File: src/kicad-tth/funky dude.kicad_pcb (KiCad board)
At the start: 2 copper layers, 57.2 x 37.5 mm, 33 parts, among them P1 CONN_2, P2 CONN_2, P3 CONN_2, SW1 SWITCH_INV, SW2 SWITCH_INV, U1 OP284

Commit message: version_2.0 initial
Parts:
- C3: value 11n -> 10n
- C6: value 50n -> 47n
- C9: value 47uf -> 47uF
- R2: value 500 -> 470

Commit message: 2014-10-22
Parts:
- removed C11: 47nf, User:C2-LARGE_PADS
- removed SW1, SW2: SWITCH_INV, User:SIL-3-LARGE_PADS
- C1, C13, C2, C3, C4, C5, C6: footprint User:C2-LARGE_PADS -> Custom:C2-LARGE_PADS
- C10, C12, C8, C9: footprint User:C1V7-LARGE_PADS -> Custom:C1V5-LARGE_PADS
- C7: value 47uf -> 1uF; footprint User:C1V7-LARGE_PADS -> Custom:C1V5-LARGE_PADS
- P1, P2, P3: footprint User:SIL-2-LARGE_PADS -> Custom:SIL-2-LARGE_PADS
- R1, R10, R11, R2, R3, R5, R6, R7, R9: footprint User:R3-LARGE_PADS -> Custom:R3-LARGE_PADS
- R4: footprint User:R4-LARGE_PADS -> Custom:R3-LARGE_PADS
- R8: value 1Meg -> 500; footprint User:R3-LARGE_PADS -> Custom:R3-LARGE_PADS
- RBASS1, RTREBLE1: footprint User:SIL-3-LARGE_PADS -> Custom:SIL-3-LARGE_PADS
- U1: footprint User:DIP-8_LARGE_PADS -> Custom:DIP-8_LARGE_PADS
- moved C12 41.7 mm to (176.5, 111.8), turned to 0 degrees
- moved RBASS1 29.5 mm to (164.5, 132.7), turned to 180 degrees
- moved C3 28.6 mm to (144.8, 130.2)
- moved R3 27.6 mm to (149.2, 120.7), turned to 270 degrees
- moved C7 25.6 mm to (148.6, 128.9)
- moved R11 21.6 mm to (167.0, 116.8), turned to 0 degrees
- moved R4 21.0 mm to (146.7, 120.7), turned to 270 degrees
- moved R6 14.8 mm to (167.0, 119.4), turned to 0 degrees
- moved C6 13.7 mm to (167.6, 122.6), turned to 0 degrees
- moved R9 11.9 mm to (175.9, 120.0), turned to 270 degrees
- moved C9 10.2 mm to (185.4, 115.6)
- moved P3 9.69 mm to (186.7, 128.3)
- moved P2 8.64 mm to (184.8, 121.3)
- moved C4 8.26 mm to (167.6, 126.4), turned to 0 degrees
- moved R10 8.13 mm to (167.0, 128.9), turned to 180 degrees
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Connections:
- C7 pad 2: Net-(C1-Pad1) -> GND
- R3 pad 2: Vref -> Net-(C7-Pad1)
- R8 pad 1: Net-(C7-Pad1) -> Net-(C4-Pad2)
- R8 pad 2: Vref -> Net-(C9-Pad1)
- RBASS1 pad 1: Net-(C9-Pad1) -> Net-(C4-Pad2)
- RBASS1 pad 2: Net-(C9-Pad1) -> Net-(C4-Pad2)
- RBASS1 pad 3: Net-(RBASS1-Pad3) -> Net-(C6-Pad1)
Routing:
- net GND: track 86.1 -> 0.00 mm
- net Net-(C1-Pad1): track 54.4 -> 4.45 mm
- net Net-(C11-Pad1): track 39.5 -> 0.00 mm
- net Net-(C6-Pad1): track 40.1 -> 19.3 mm
- net Net-(C3-Pad2): track 34.0 -> 14.9 mm
- net Net-(C7-Pad1): track 20.9 -> 3.44 mm
- net Net-(RBASS1-Pad3): track 15.8 -> 0.00 mm
- net Vref: track 49.5 -> 35.1 mm
- net Net-(C2-Pad1): track 38.8 -> 28.9 mm
- net Net-(C1-Pad2): track 11.7 -> 21.3 mm
- net Net-(C3-Pad1): track 13.2 -> 3.96 mm
- net Net-(C9-Pad1): track 19.2 -> 10.5 mm
- net +9V: track 55.3 -> 48.9 mm
- net Net-(C4-Pad2): track 72.1 -> 67.4 mm
- net Net-(C2-Pad2): track 28.6 -> 31.2 mm
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- added copper zone on F.Cu, net GND
- removed copper zone on B.Cu, net GND
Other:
- board size 57.2 x 37.5 mm -> 52.1 x 29.8 mm
- net class Default: clearance 0.508 -> 0.381; trace_width 0.762 -> 0.508; via_dia 1.016 -> 0.762; via_drill 0.635 -> 0.508
- rule trace_clearance: 0.508 -> 0.381
- board text added: "V2.0-t"
- board text added: "funky dude preamp v2.0-t www.dolganoff.com"
- board text removed: "V1-t"
- board text removed: "funky dude preamp v1-t www.dolganoff.com"

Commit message: 2014-10-23
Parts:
- moved P3 18.5 mm to (181.2, 110.6), turned to 180 degrees
- moved C13 6.87 mm to (178.4, 125.7), turned to 180 degrees
- moved C9 4.19 mm to (181.2, 115.7)
- moved C3 3.69 mm to (148.5, 130.3), turned to 0 degrees
- moved R8 3.52 mm to (177.2, 119.1), turned to 90 degrees
- moved R1 3.31 mm to (157.4, 120.4)
- moved R7 3.00 mm to (157.4, 123.3)
- moved C5 2.84 mm to (156.8, 126.4)
- moved C7 2.79 mm to (149.7, 126.4)
- moved C4 2.79 mm to (168.8, 123.8)
- moved U1 2.79 mm to (157.4, 113.0)
- moved C1 2.74 mm to (142.6, 118.1)
- moved R10 2.74 mm to (168.0, 126.4)
- moved RBASS1 2.73 mm to (165.7, 130.3)
- moved RTREBLE1 2.73 mm to (156.8, 130.3)
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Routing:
- net Net-(C4-Pad2): track 67.4 -> 57.1 mm
- net Vref: track 35.1 -> 26.8 mm
- net Net-(C9-Pad1): track 10.5 -> 2.83 mm
- net Net-(C3-Pad2): track 14.9 -> 9.82 mm
- net Net-(C3-Pad1): track 3.96 -> 8.79 mm
- net Net-(C12-Pad1): track 7.07 -> 5.09 mm
- net +9V: track 48.9 -> 47.5 mm
- net Net-(C1-Pad2): track 21.3 -> 20.1 mm
- net Net-(C9-Pad2): track 5.23 -> 4.68 mm
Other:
- board size 52.1 x 29.8 mm -> 45.2 x 27.9 mm
- board text added: "+"
- board text added: "Licenced under CERN OHL v1.2"
- board text added: "Open Hardware"
- board text added: "bass"
- board text added: "in"
- board text added: "out"
- board text added: "treble"
- board text removed: "V2.0-t"

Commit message: 2014-10-23.2 - PCB is routed
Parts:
- moved C10 0.63 mm to (178.7, 130.4)
- moved C9 0.51 mm to (181.2, 116.2)
- moved P3 0.51 mm to (181.2, 111.1)
- moved C1 0.46 mm to (142.4, 118.5)
- moved R3 0.36 mm to (150.0, 118.5)
- moved C4 0.36 mm to (168.5, 124.1)
- moved R4 0.36 mm to (147.4, 119.0)
- moved C6 0.28 mm to (168.5, 120.3)
- moved RGAIN1 0.28 mm to (147.4, 109.3)
- moved C13 0.28 mm to (178.2, 125.9)
- moved P2 0.25 mm to (182.2, 121.8)
- moved R10 0.25 mm to (168.0, 126.6)
- moved C2 0.25 mm to (167.3, 109.3)
- moved R11 0.25 mm to (168.5, 114.4)
- moved R2 0.25 mm to (144.9, 118.7)
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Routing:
- net Net-(C1-Pad2): track 20.1 -> 21.5 mm
- net Net-(C2-Pad2): track 31.0 -> 32.1 mm
- net +9V: track 47.5 -> 48.5 mm
- net Net-(C4-Pad1): track 41.9 -> 42.7 mm
- net Net-(C4-Pad2): track 57.1 -> 57.9 mm
- net Net-(C2-Pad1): track 28.5 -> 29.2 mm
- net Net-(C6-Pad1): track 19.4 -> 18.7 mm
- net Net-(C3-Pad1): track 8.79 -> 8.25 mm

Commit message: 2014-11-02 pcb changes
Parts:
- moved RBASS1 0.51 mm to (165.7, 129.9)
- moved RTREBLE1 0.51 mm to (156.8, 129.9)
- moved C13 0.25 mm to (178.2, 126.1)
- moved C4 0.25 mm to (168.5, 123.8)
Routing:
- net +9V: track 48.5 -> 23.4 mm
- net Net-(C4-Pad1): track 42.7 -> 40.9 mm
- net Net-(C5-Pad1): track 3.94 -> 3.43 mm
- added copper zone on B.Cu, net +9V
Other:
- outline, holes or cut-outs redrawn

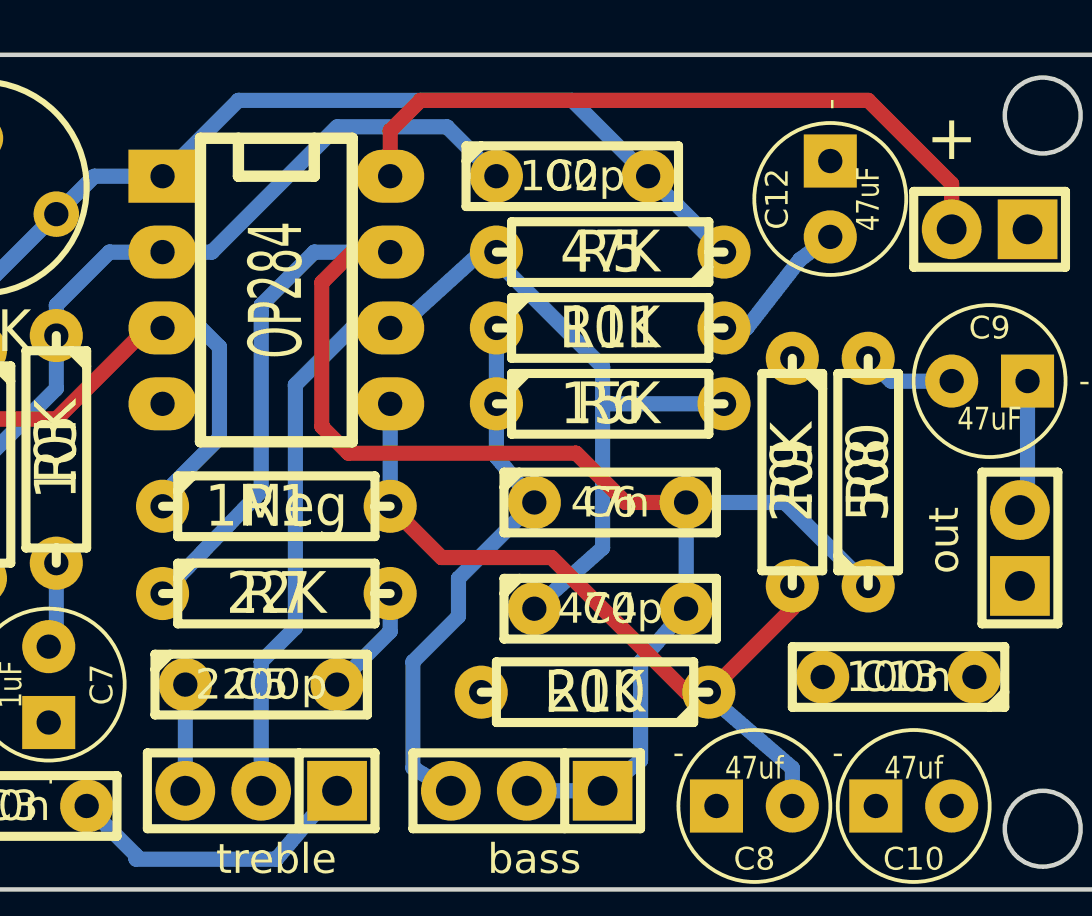
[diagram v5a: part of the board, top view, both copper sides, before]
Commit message: change to TLC2262
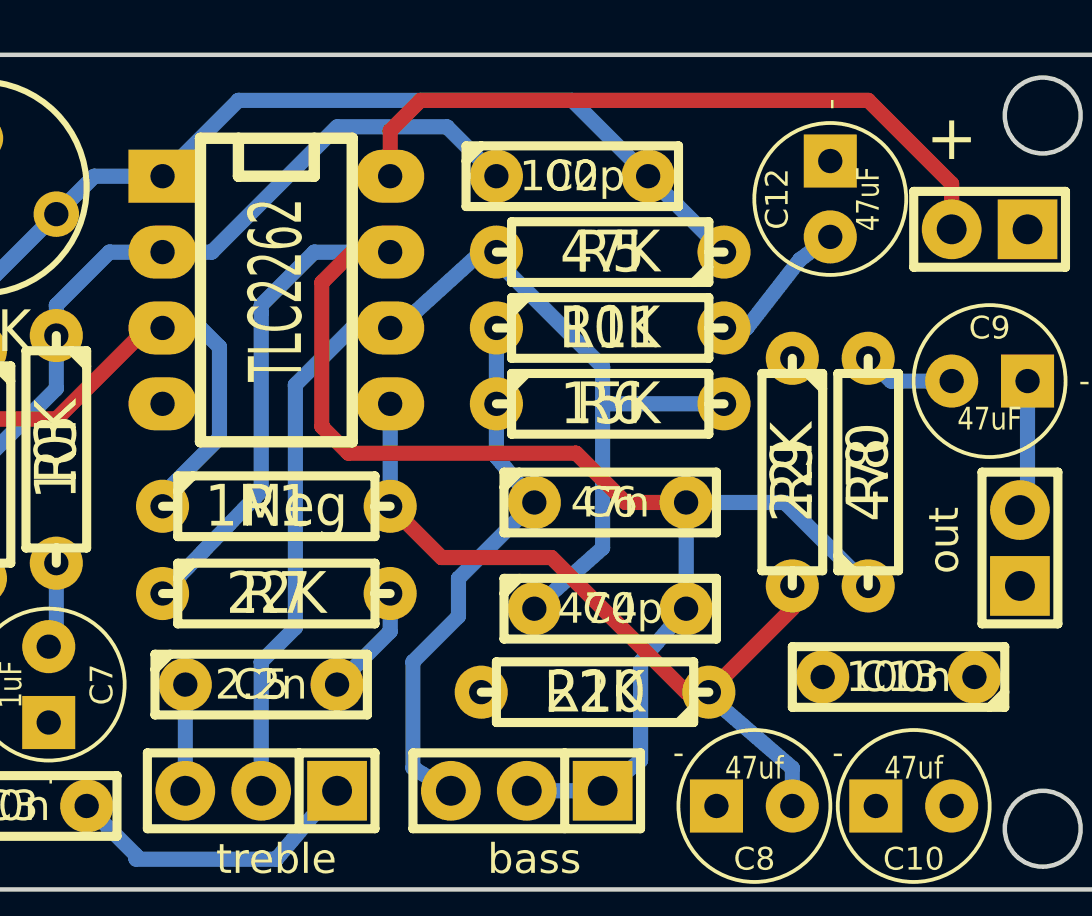
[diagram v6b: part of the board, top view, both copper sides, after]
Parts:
- C5: value 2200p -> 2.2n
- R10, R9: value 20K -> 22K
- R8: value 500 -> 470
- U1: value OP284 -> TLC2262

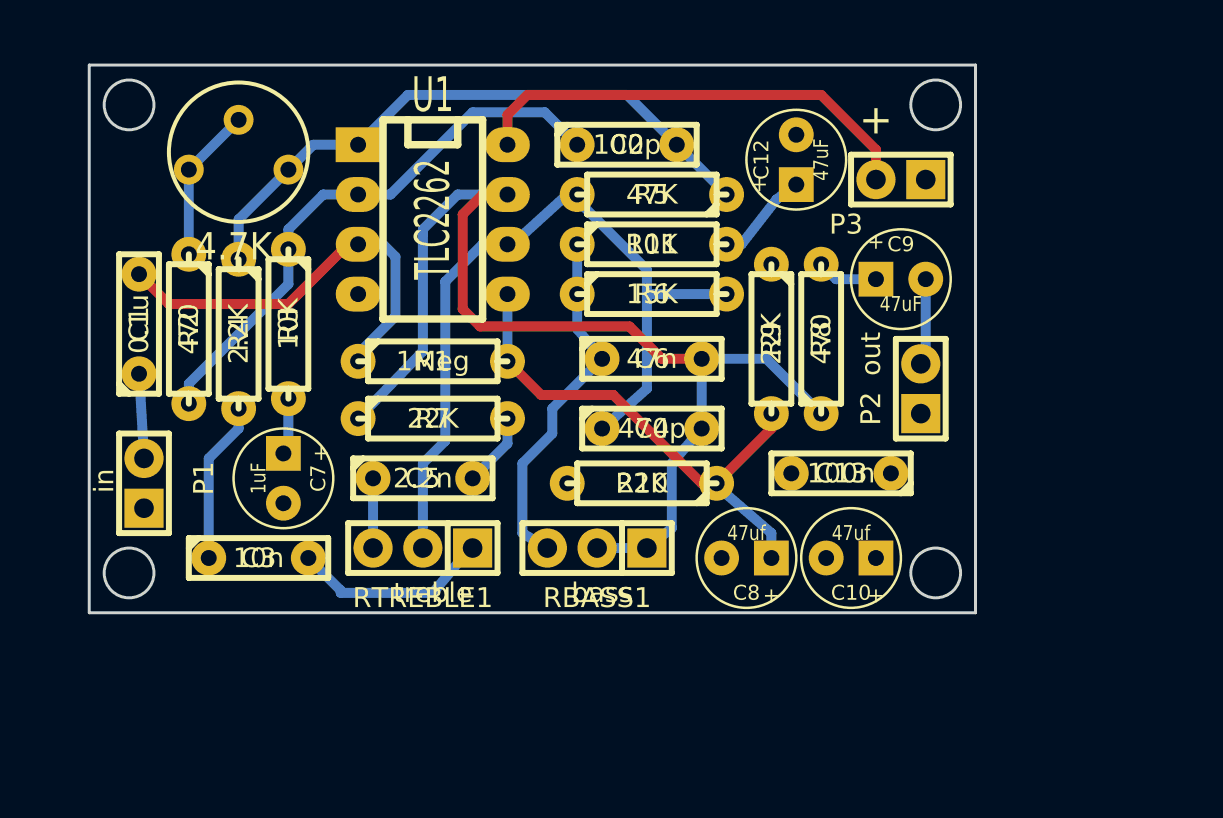
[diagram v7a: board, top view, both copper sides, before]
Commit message: smaller bcb design, removed gain trim
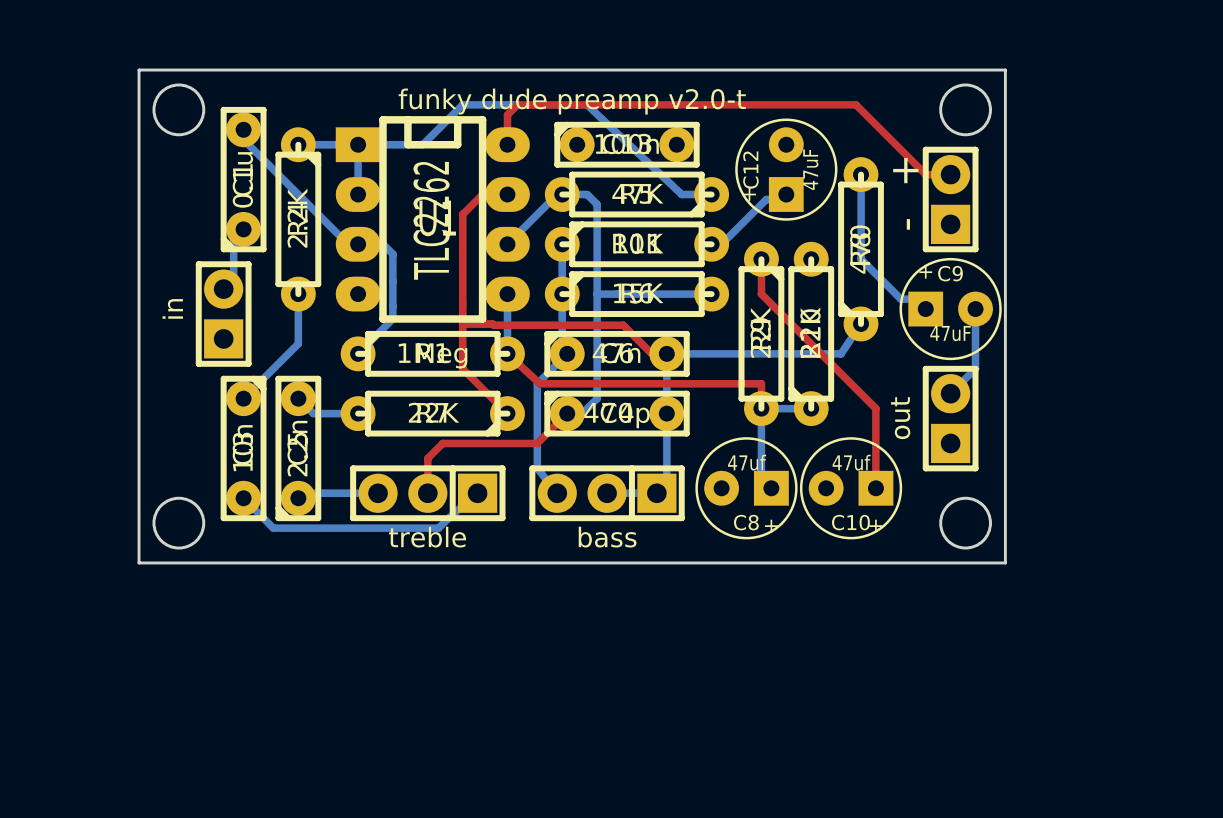
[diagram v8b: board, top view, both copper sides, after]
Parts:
- removed C2: 100p, Custom:C2-LARGE_PADS
- removed C7: 1uF, Custom:C1V5-LARGE_PADS
- removed R2: 470, Custom:R3-LARGE_PADS
- removed R3: 10K, Custom:R3-LARGE_PADS
- removed RGAIN1: 4.7K, Discret:RV2
- moved C13 20.0 mm to (167.3, 109.3), turned to 0 degrees
- moved R10 11.5 mm to (176.7, 119.0), turned to 90 degrees
- moved P1 9.54 mm to (146.7, 118.0)
- moved C1 9.09 mm to (147.7, 111.1)
- moved R4 6.59 mm to (150.5, 113.2)
- moved C5 6.53 mm to (150.5, 124.8), turned to 90 degrees
- moved C3 5.64 mm to (147.7, 124.8), turned to 270 degrees
- moved R8 5.00 mm to (179.2, 114.7)
- moved C10 3.56 mm to (178.7, 126.9)
- moved C8 3.56 mm to (173.4, 126.9)
- moved C9 2.96 mm to (183.8, 117.7)
- moved RBASS1 2.84 mm to (166.2, 127.1)
- moved RTREBLE1 2.81 mm to (157.1, 127.1)
- moved P3 2.74 mm to (183.8, 112.1), turned to 90 degrees
- moved P2 2.16 mm to (183.8, 123.3)
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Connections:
- R4 pad 1: Net-(C2-Pad2) -> Net-(R4-Pad1)
- R5 pad 1: Net-(C2-Pad2) -> Net-(R4-Pad1)
- U1 pad 1: Net-(C2-Pad2) -> Net-(R4-Pad1)
- U1 pad 2: Net-(C2-Pad1) -> Net-(R4-Pad1)
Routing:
- net Net-(C2-Pad2): track 31.7 -> 0.00 mm
- net Net-(C2-Pad1): track 28.9 -> 0.00 mm
- net Net-(R4-Pad1): track 0.00 -> 26.3 mm
- net +9V: track 23.4 -> 39.9 mm
- net Net-(C4-Pad2): track 57.5 -> 45.9 mm
- net Net-(R2-Pad1): track 7.91 -> 0.00 mm
- net Net-(C4-Pad1): track 40.9 -> 33.5 mm
- net Net-(C9-Pad1): track 3.11 -> 8.67 mm
- net Net-(C1-Pad2): track 21.5 -> 16.5 mm
- net Net-(C6-Pad1): track 18.4 -> 13.8 mm
- net Net-(C3-Pad2): track 10.3 -> 13.2 mm
- net Net-(C7-Pad1): track 2.90 -> 0.00 mm
- net Net-(C3-Pad1): track 8.25 -> 6.49 mm
- net Vref: track 26.3 -> 24.7 mm
- net Net-(C1-Pad1): track 4.33 -> 3.47 mm
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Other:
- board size 45.2 x 27.9 mm -> 44.2 x 25.1 mm
- net class Default: trace_width 0.508 -> 0.381
- rule trace_min: 0.508 -> 0.381
- board text added: "-"
- board text added: "funky dude preamp v2.0-t"
- board text added: "www.dolganoff.com/fr/a-propos"
- board text removed: "funky dude preamp v2.0-t www.dolganoff.com"
